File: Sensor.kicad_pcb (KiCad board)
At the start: 2 copper layers, 49 x 49 mm, 79 parts, among them IC1 STM32L051K8T6, P1 CONN_02X04, P2 CONN_02X04, P3 CONN_01X02, Q1 AO3401, Q2 NMosfetGen, Q3 NMosfetGen, Q4 Q_NMOS_GSD, SW1 SW_PUSH, SW2 SW_PUSH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

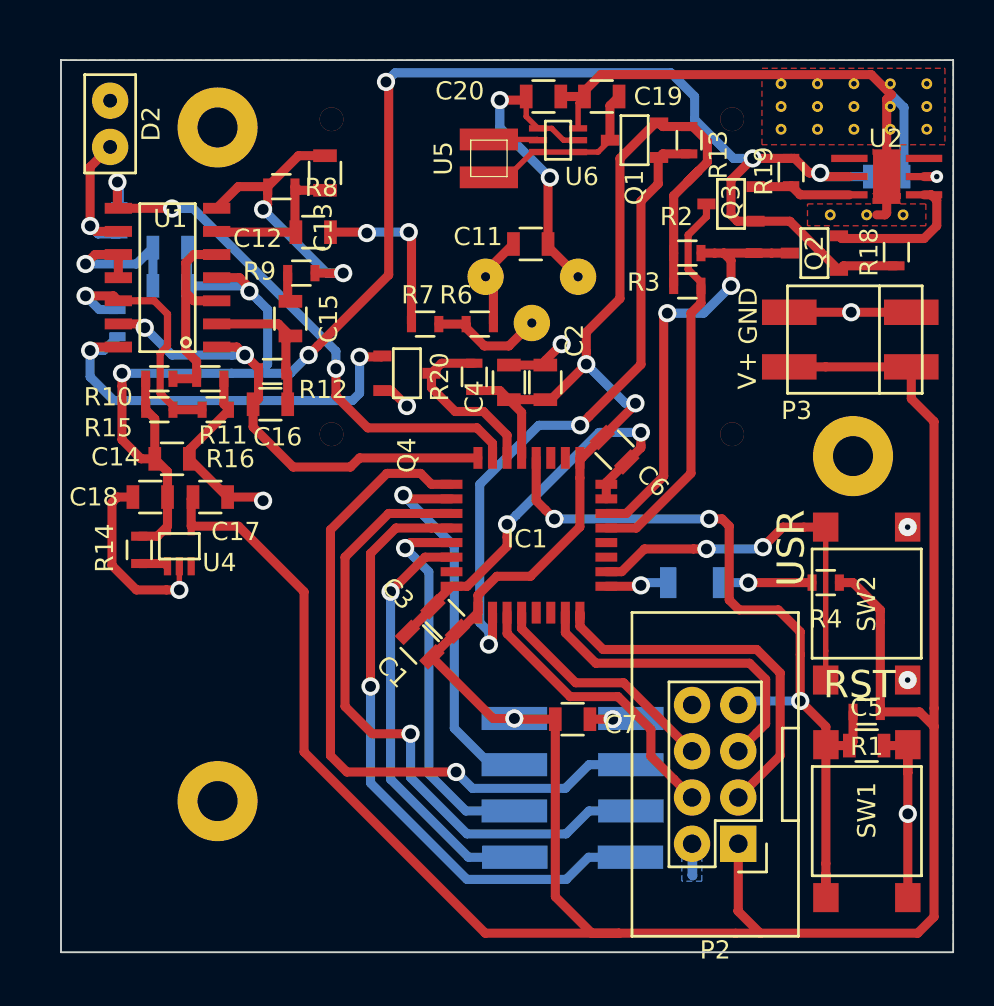
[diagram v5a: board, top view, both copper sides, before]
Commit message: Add url to open source project on silkscreens
Signed-off-by: Philip Luyckx <philip.luyckx@gmail.com>
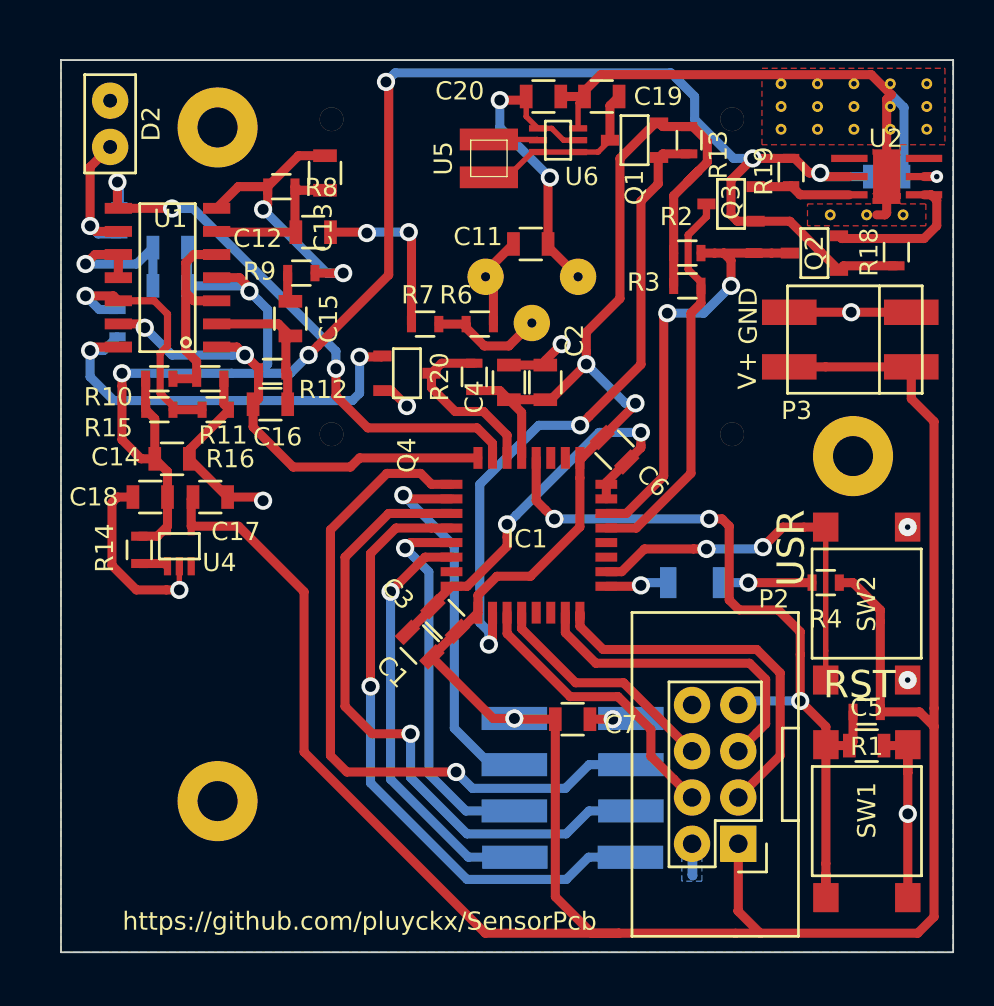
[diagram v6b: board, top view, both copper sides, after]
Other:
- board text added: "https://github.com/pluyckx/SensorPcb"
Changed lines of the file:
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@@
     (area 115.403143 56.1 188.147166 119.211)
     (thickness 1.6)
-    (drawings 18)
+    (drawings 20)
     (tracks 582)
     (zones 0)
@@
     (descr "Through hole pin header")
     (tags "pin header")
-    (fp_text reference P2 (at 1.27 -5.842 180) (layer F.SilkS)
+    (fp_text reference P2 (at -1.95 13.44 180) (layer F.SilkS)
       (effects (font (size 1 1) (thickness 0.15)))
     )
@@
       (clearance 0.5))
   )
+  (gr_text https://github.com/pluyckx/SensorPcb (at 134.55 116.55) (layer B.SilkS)
+    (effects (font (size 1 1) (thickness 0.2)) (justify mirror))
+  )
+  (gr_text https://github.com/pluyckx/SensorPcb (at 134.6 116.5) (layer F.SilkS)
+    (effects (font (size 1 1) (thickness 0.2)))
+  )
   (gr_text GND (at 155.95 83.25 90) (layer F.SilkS)
